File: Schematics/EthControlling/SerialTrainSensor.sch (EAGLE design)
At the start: 18 parts, among them IC1 ATTINY10, IC2 LMV358, IC3 ATTINY10

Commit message: restore repository
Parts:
- removed JP1, JP2: SERIAL_SENSOR, myparts:SERIAL_SENSOR
- added SMD1, SMD2: SERIAL_SENSORTH, myparts:SERIAL_SENSORTH
- renumbered IC1 to U$1, IC3 to U$2
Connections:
- net CHAIN_IN: now also SMD2.CHAIN; no longer JP2.CHAIN
- net CHAIN_OUT: now also SMD1.CHAIN; no longer JP1.CHAIN
- net GND: now also R5.1, SMD1.GND, SMD2.GND; no longer JP1.GND, JP2.GND, R3.1, R4.1, R5.2, U$100.2, U$101.2
- net SENS_A: now also R3.1
- net SENS_B: now also R4.1, R5.2; no longer R5.1
- net TRANS: now also SMD1.TRANS, SMD2.TRANS; no longer JP1.TRANS, JP2.TRANS
- net VCC: now also D1.A, D2.A, SMD1.VCC, SMD2.VCC; no longer JP1.VCC, JP2.VCC
- net VLED: now also SMD1.VLED, SMD2.VLED, U$100.2, U$101.2; no longer D1.A, D2.A, JP1.VLED, JP2.VLED
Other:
- moved on the sheet: R1, R4, R5

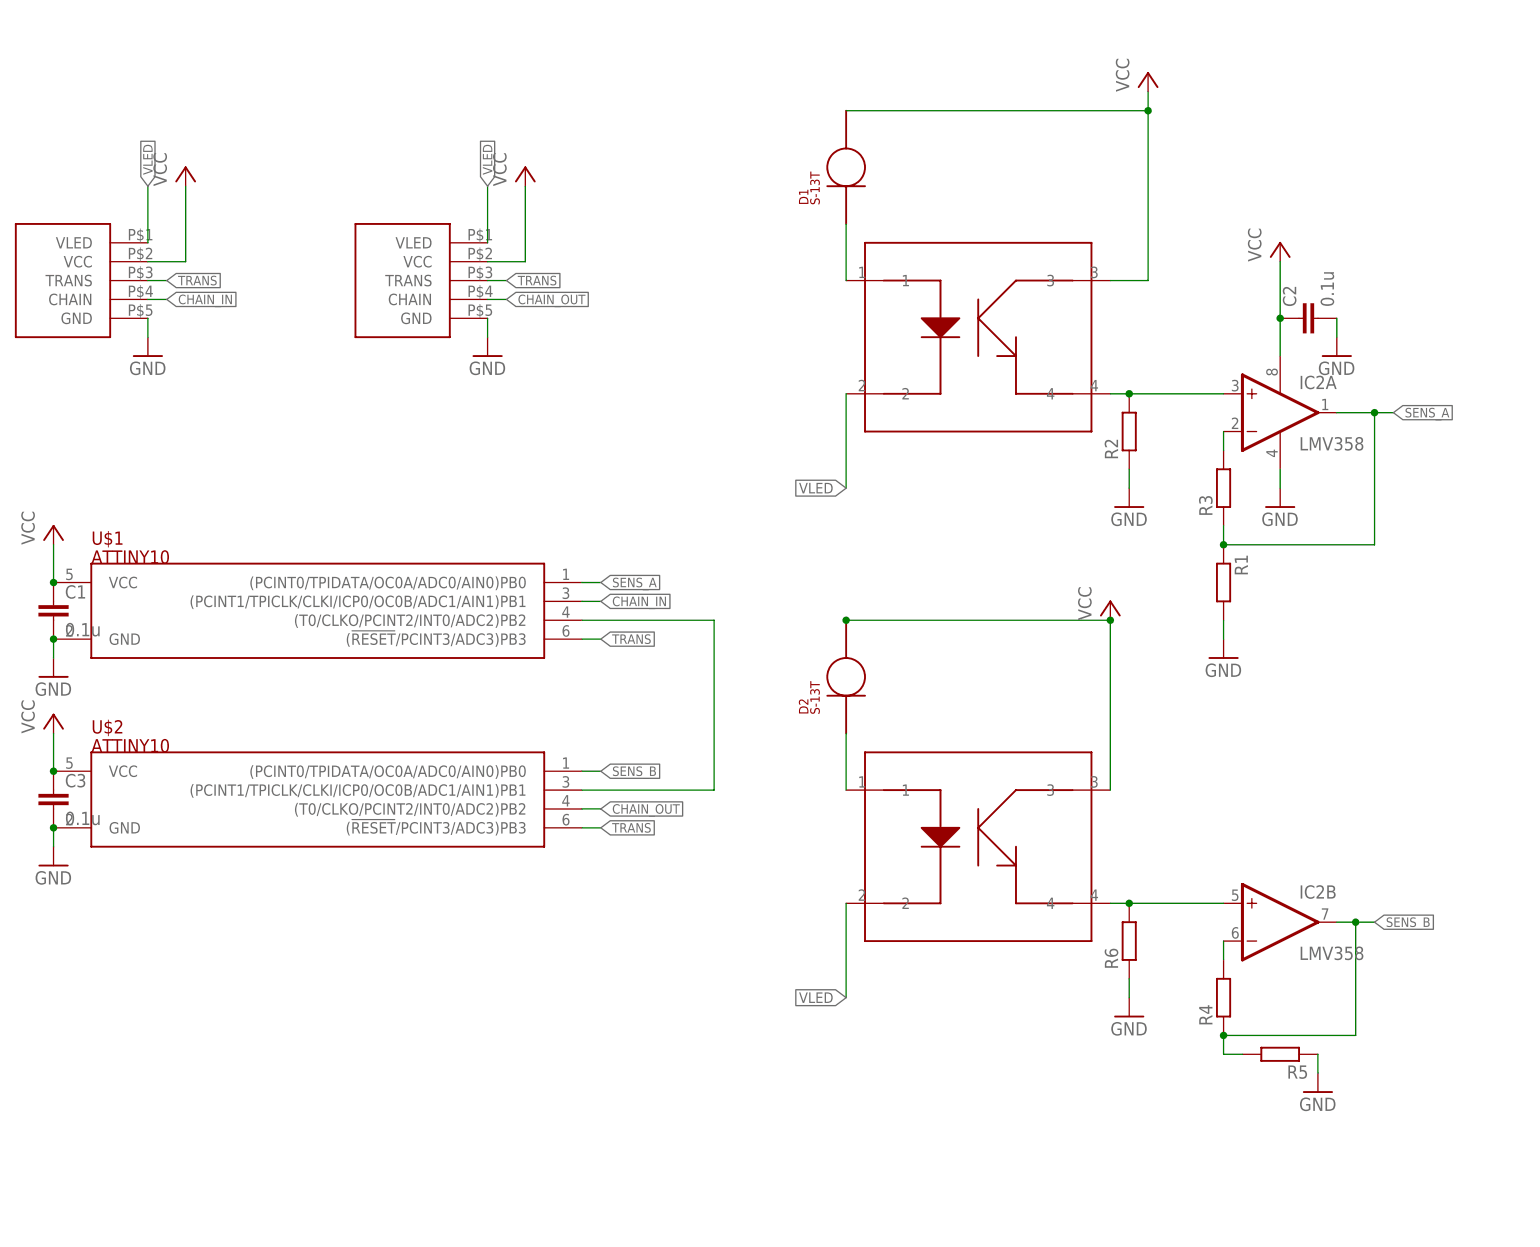
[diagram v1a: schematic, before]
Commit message: wired SerialTrainSensor RevB
Signed-off-by: sosoru <siva6991@yahoo.co.jp>
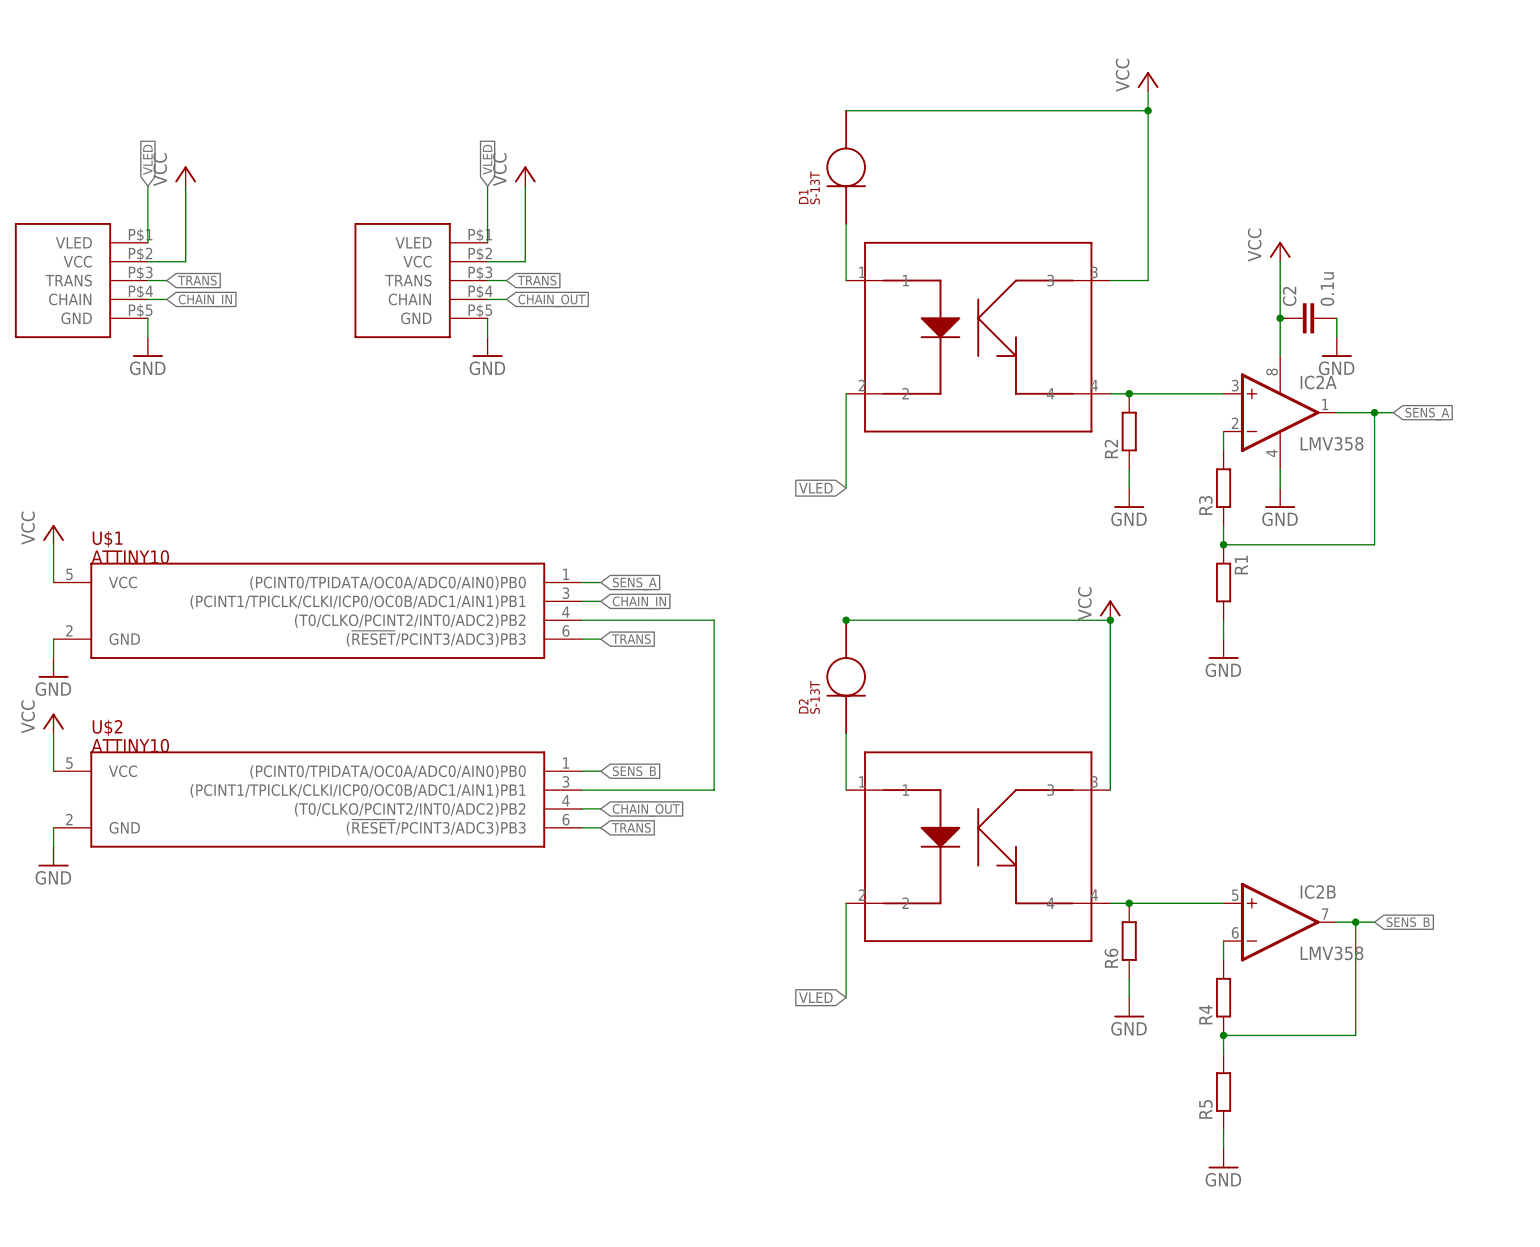
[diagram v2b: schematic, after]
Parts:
- removed C1, C3: 0.1u, rcl:C-EUC0603
- SMD1, SMD2: value SERIAL_SENSORTH -> SERIAL_SENSORHALF; device myparts:SERIAL_SENSORTH -> myparts:SERIAL_SENSORHALF
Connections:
- net CHAIN_IN: now also SMD1.CHAIN; no longer SMD2.CHAIN
- net CHAIN_OUT: now also SMD2.CHAIN; no longer SMD1.CHAIN
- net GND: no longer C1.2, C3.2
- net VCC: no longer C1.1, C3.1
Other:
- moved on the sheet: R5
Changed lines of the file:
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@@
 <part name="U$100" library="myparts" deviceset="TPR-105F" device=""/>
 <part name="D2" library="myparts" deviceset="S-1*3T" device=""/>
-<part name="C1" library="rcl" deviceset="C-EU" device="C0603" value="0.1u"/>
-<part name="C3" library="rcl" deviceset="C-EU" device="C0603" value="0.1u"/>
 <part name="GND7" library="supply1" deviceset="GND" device=""/>
 <part name="R3" library="rcl" deviceset="R-EU_" device="R0603"/>
@@
 <part name="GND12" library="supply1" deviceset="GND" device=""/>
 <part name="IC2" library="myparts" deviceset="LMV358?*" device=""/>
-<part name="SMD1" library="myparts" deviceset="SERIAL_SENSOR" device="TH"/>
-<part name="SMD2" library="myparts" deviceset="SERIAL_SENSOR" device="TH"/>
 <part name="U$1" library="myparts" deviceset="ATTINY10" device=""/>
 <part name="U$2" library="myparts" deviceset="ATTINY10" device=""/>
+<part name="SMD1" library="myparts" deviceset="SERIAL_SENSOR" device="HALF"/>
+<part name="SMD2" library="myparts" deviceset="SERIAL_SENSOR" device="HALF"/>
 </parts>
 <sheets>
@@
 <instance part="U$100" gate="G$1" x="134.62" y="17.78"/>
 <instance part="D2" gate="G$1" x="109.22" y="50.8" rot="R90"/>
-<instance part="C1" gate="G$1" x="2.54" y="58.42"/>
-<instance part="C3" gate="G$1" x="2.54" y="33.02"/>
 <instance part="GND7" gate="1" x="167.64" y="71.12"/>
 <instance part="R3" gate="G$1" x="160.02" y="73.66" rot="R90"/>
@@
 <instance part="GND10" gate="1" x="147.32" y="2.54"/>
 <instance part="R4" gate="G$1" x="160.02" y="5.08" rot="R90"/>
-<instance part="R5" gate="G$1" x="167.64" y="-2.54" rot="R180"/>
-<instance part="GND11" gate="1" x="172.72" y="-7.62"/>
+<instance part="R5" gate="G$1" x="160.02" y="-7.62" rot="R90"/>
+<instance part="GND11" gate="1" x="160.02" y="-17.78"/>
 <instance part="P+1" gate="VCC" x="20.32" y="116.84"/>
 <instance part="P+9" gate="VCC" x="66.04" y="116.84"/>
@@
 <instance part="IC2" gate="P" x="167.64" y="83.82"/>
 <instance part="IC2" gate="B" x="167.64" y="15.24"/>
-<instance part="SMD1" gate="G$1" x="55.88" y="99.06"/>
-<instance part="SMD2" gate="G$1" x="10.16" y="99.06"/>
 <instance part="U$1" gate="G$1" x="40.64" y="55.88"/>
 <instance part="U$2" gate="G$1" x="40.64" y="30.48"/>
+<instance part="SMD1" gate="G$1" x="10.16" y="99.06"/>
+<instance part="SMD2" gate="G$1" x="55.88" y="99.06"/>
 </instances>
 <busses>
@@
 <wire x1="15.24" y1="101.6" x2="17.78" y2="101.6" width="0.1524" layer="91"/>
 <label x="17.78" y="101.6" size="1.27" layer="95" xref="yes"/>
-<pinref part="SMD2" gate="G$1" pin="TRANS"/>
+<pinref part="SMD1" gate="G$1" pin="TRANS"/>
 </segment>
 <segment>
 <wire x1="60.96" y1="101.6" x2="63.5" y2="101.6" width="0.1524" layer="91"/>
 <label x="63.5" y="101.6" size="1.27" layer="95" xref="yes"/>
-<pinref part="SMD1" gate="G$1" pin="TRANS"/>
+<pinref part="SMD2" gate="G$1" pin="TRANS"/>
 </segment>
 <segment>
@@
 <wire x1="17.78" y1="99.06" x2="15.24" y2="99.06" width="0.1524" layer="91"/>
 <label x="17.78" y="99.06" size="1.27" layer="95" xref="yes"/>
-<pinref part="SMD2" gate="G$1" pin="CHAIN"/>
+<pinref part="SMD1" gate="G$1" pin="CHAIN"/>
 </segment>
 <segment>
@@
 <wire x1="60.96" y1="99.06" x2="63.5" y2="99.06" width="0.1524" layer="91"/>
 <label x="63.5" y="99.06" size="1.27" layer="95" xref="yes"/>
-<pinref part="SMD1" gate="G$1" pin="CHAIN"/>
+<pinref part="SMD2" gate="G$1" pin="CHAIN"/>
 </segment>
 <segment>
@@
 <pinref part="GND1" gate="1" pin="GND"/>
 <wire x1="15.24" y1="96.52" x2="15.24" y2="93.98" width="0.1524" layer="91"/>
-<pinref part="SMD2" gate="G$1" pin="GND"/>
+<pinref part="SMD1" gate="G$1" pin="GND"/>
 </segment>
 <segment>
 <pinref part="GND2" gate="1" pin="GND"/>
 <wire x1="60.96" y1="96.52" x2="60.96" y2="93.98" width="0.1524" layer="91"/>
-<pinref part="SMD1" gate="G$1" pin="GND"/>
+<pinref part="SMD2" gate="G$1" pin="GND"/>
 </segment>
 <segment>
 <pinref part="GND3" gate="1" pin="GND"/>
 <wire x1="2.54" y1="50.8" x2="2.54" y2="53.34" width="0.1524" layer="91"/>
-<pinref part="C1" gate="G$1" pin="2"/>
 <pinref part="U$1" gate="G$1" pin="GND"/>
-<junction x="2.54" y="53.34"/>
 </segment>
 <segment>
 <pinref part="GND4" gate="1" pin="GND"/>
 <wire x1="2.54" y1="27.94" x2="2.54" y2="25.4" width="0.1524" layer="91"/>
-<pinref part="C3" gate="G$1" pin="2"/>
 <pinref part="U$2" gate="G$1" pin="GND"/>
-<junction x="2.54" y="27.94"/>
 </segment>
 <segment>
@@
 <pinref part="R5" gate="G$1" pin="1"/>
 <pinref part="GND11" gate="1" pin="GND"/>
-<wire x1="172.72" y1="-2.54" x2="172.72" y2="-5.08" width="0.1524" layer="91"/>
+<wire x1="160.02" y1="-15.24" x2="160.02" y2="-12.7" width="0.1524" layer="91"/>
 </segment>
 </net>
@@
 <pinref part="R4" gate="G$1" pin="1"/>
 <wire x1="177.8" y1="15.24" x2="180.34" y2="15.24" width="0.1524" layer="91"/>
-<wire x1="162.56" y1="-2.54" x2="160.02" y2="-2.54" width="0.1524" layer="91"/>
 <wire x1="160.02" y1="-2.54" x2="160.02" y2="0" width="0.1524" layer="91"/>
 <wire x1="160.02" y1="0" x2="177.8" y2="0" width="0.1524" layer="91"/>
@@
 <wire x1="15.24" y1="104.14" x2="20.32" y2="104.14" width="0.1524" layer="91"/>
 <wire x1="20.32" y1="104.14" x2="20.32" y2="114.3" width="0.1524" layer="91"/>
-<pinref part="SMD2" gate="G$1" pin="VCC"/>
+<pinref part="SMD1" gate="G$1" pin="VCC"/>
 </segment>
 <segment>
@@
 <wire x1="60.96" y1="104.14" x2="66.04" y2="104.14" width="0.1524" layer="91"/>
 <wire x1="66.04" y1="104.14" x2="66.04" y2="114.3" width="0.1524" layer="91"/>
-<pinref part="SMD1" gate="G$1" pin="VCC"/>
+<pinref part="SMD2" gate="G$1" pin="VCC"/>
 </segment>
 <segment>
 <wire x1="2.54" y1="66.04" x2="2.54" y2="60.96" width="0.1524" layer="91"/>
-<pinref part="C1" gate="G$1" pin="1"/>
 <pinref part="P+3" gate="VCC" pin="VCC"/>
 <pinref part="U$1" gate="G$1" pin="VCC"/>
-<junction x="2.54" y="60.96"/>
 </segment>
 <segment>
 <wire x1="2.54" y1="40.64" x2="2.54" y2="35.56" width="0.1524" layer="91"/>
-<pinref part="C3" gate="G$1" pin="1"/>
 <pinref part="P+4" gate="VCC" pin="VCC"/>
 <pinref part="U$2" gate="G$1" pin="VCC"/>
-<junction x="2.54" y="35.56"/>
 </segment>
 <segment>
@@
 <wire x1="15.24" y1="114.3" x2="15.24" y2="106.68" width="0.1524" layer="91"/>
 <label x="15.24" y="114.3" size="1.27" layer="95" rot="R90" xref="yes"/>
-<pinref part="SMD2" gate="G$1" pin="VLED"/>
+<pinref part="SMD1" gate="G$1" pin="VLED"/>
 </segment>
 <segment>
 <wire x1="60.96" y1="114.3" x2="60.96" y2="106.68" width="0.1524" layer="91"/>
 <label x="60.96" y="114.3" size="1.27" layer="95" rot="R90" xref="yes"/>
-<pinref part="SMD1" gate="G$1" pin="VLED"/>
-</segment>
-<segment>
+<pinref part="SMD2" gate="G$1" pin="VLED"/>
+</segment>
+<segment>

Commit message: ditto
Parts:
- added R7: (no value), rcl:R-EU_R0603
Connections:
- net N$4: now also R7.2
- net VCC: now also R7.1
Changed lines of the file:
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@@
 <part name="SMD1" library="myparts" deviceset="SERIAL_SENSOR" device="HALF"/>
 <part name="SMD2" library="myparts" deviceset="SERIAL_SENSOR" device="HALF"/>
+<part name="R7" library="rcl" deviceset="R-EU_" device="R0603"/>
+<part name="P+2" library="supply1" deviceset="VCC" device=""/>
 </parts>
 <sheets>
@@
 <instance part="SMD1" gate="G$1" x="10.16" y="99.06"/>
 <instance part="SMD2" gate="G$1" x="55.88" y="99.06"/>
+<instance part="R7" gate="G$1" x="91.44" y="60.96" rot="R270"/>
+<instance part="P+2" gate="VCC" x="91.44" y="68.58"/>
 </instances>
 <busses>
@@
 <pinref part="U$1" gate="G$1" pin="(T0/CLKO/PCINT2/INT0/ADC2)PB2"/>
 <pinref part="U$2" gate="G$1" pin="(PCINT1/TPICLK/CLKI/ICP0/OC0B/ADC1/AIN1)PB1"/>
+<pinref part="R7" gate="G$1" pin="2"/>
+<junction x="91.44" y="55.88"/>
 </segment>
 </net>
@@
 <pinref part="IC2" gate="P" pin="V+"/>
 </segment>
-</net>
+<segment>
+<pinref part="R7" gate="G$1" pin="1"/>
+<pinref part="P+2" gate="VCC" pin="VCC"/>
+</segment>
+</net>
